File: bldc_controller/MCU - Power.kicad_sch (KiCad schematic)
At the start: 11 parts, among them U1 STM32G474RET3

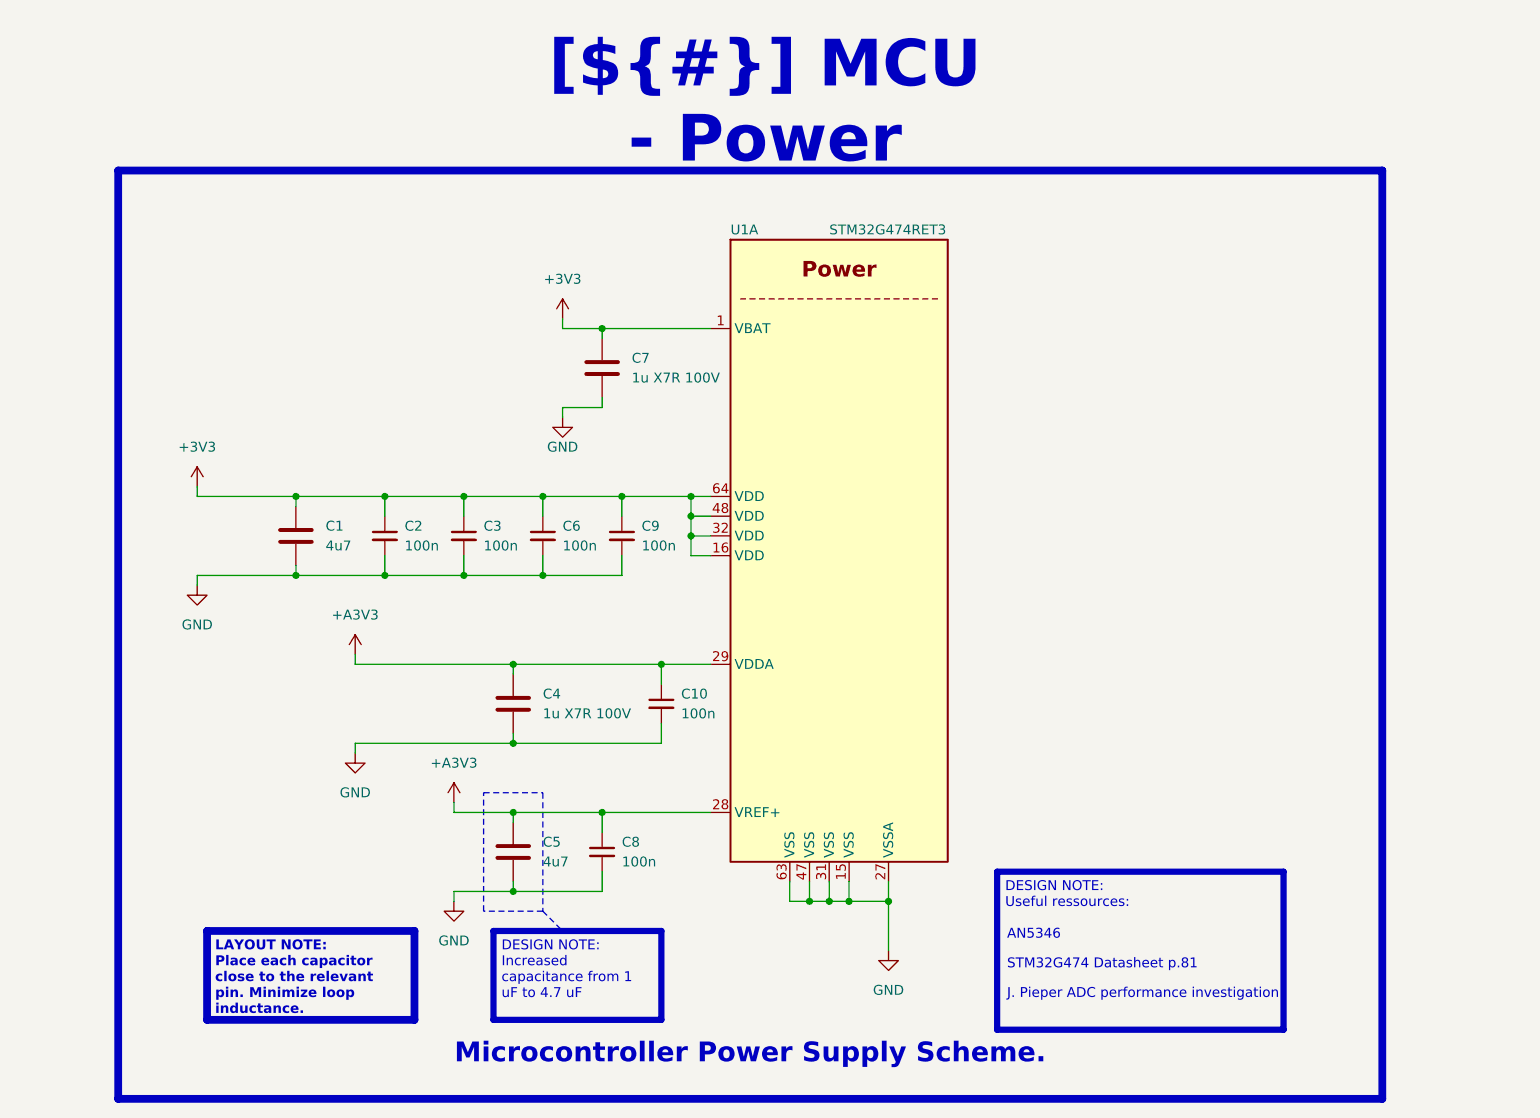
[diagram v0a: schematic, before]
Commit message: schematic is complete. Replaced 5V buck and added pi filters.
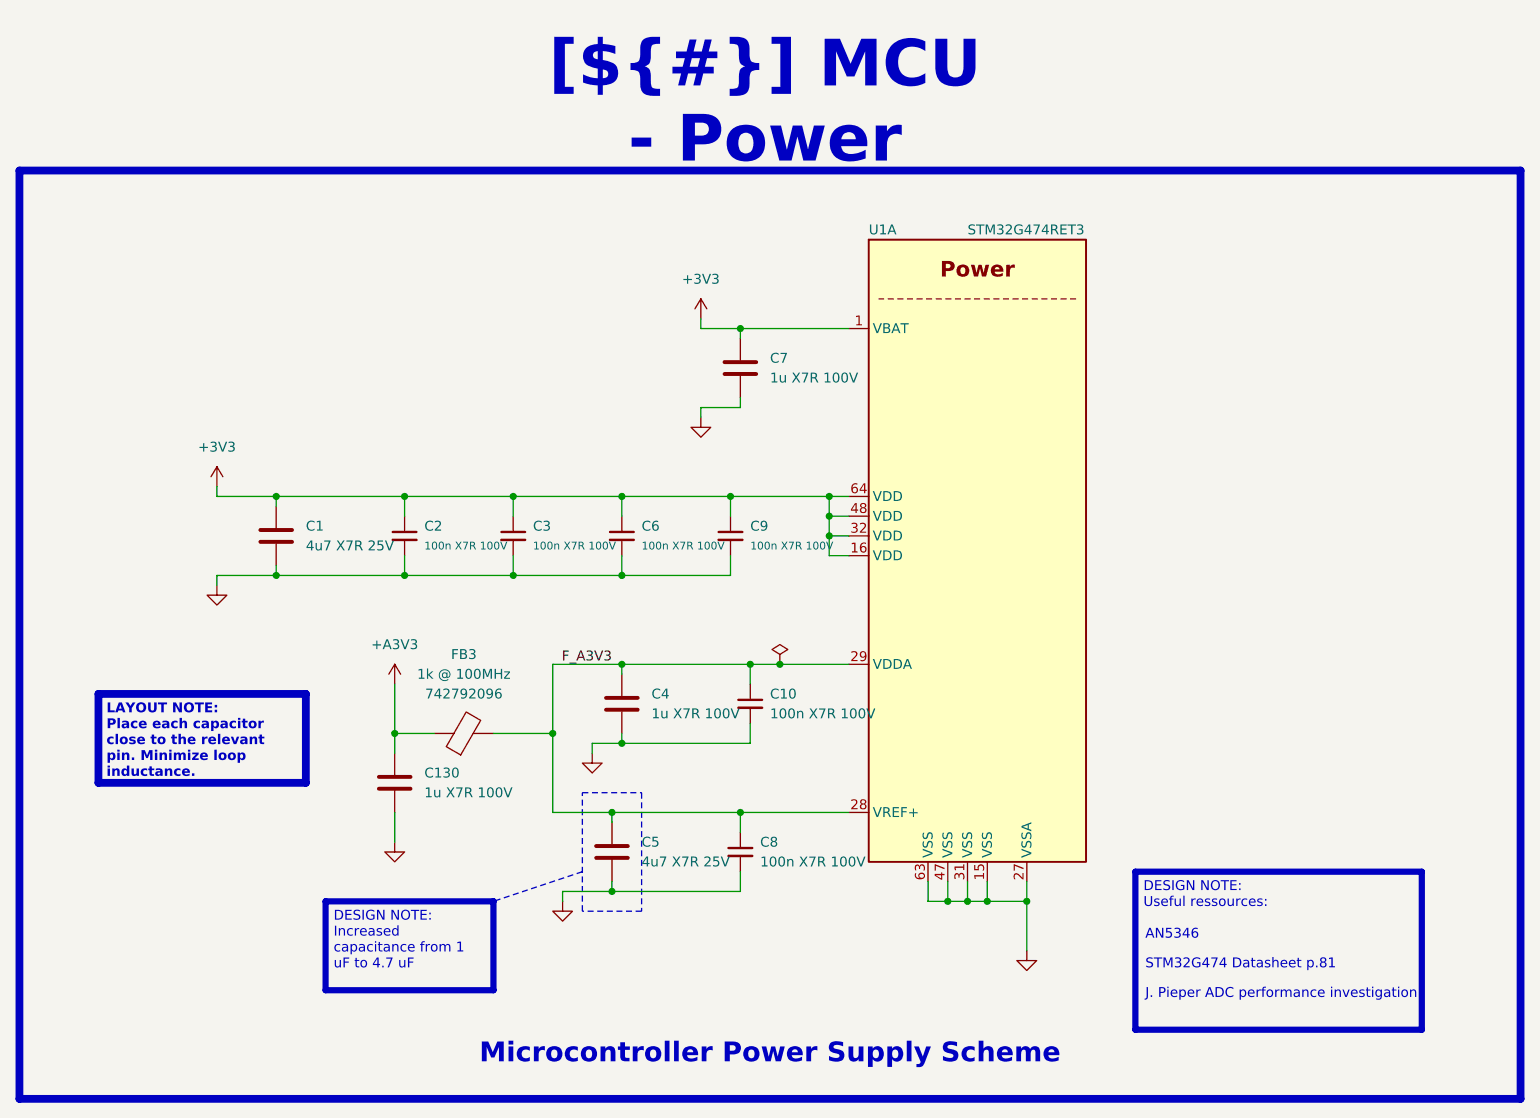
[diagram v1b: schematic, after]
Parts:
- added C130: 1u X7R 100V, 0_capacitor_smd:C_0402_1005_DensityHigh, symbol Device:C
- added FB3: 1k @ 100MHz, 0_resistor_smd:R_0805_2012_DensityHigh, symbol Device:FerriteBead
- C1, C5: value 4u7 -> 4u7 X7R 25V
- C10, C2, C3, C6, C8, C9: value 100n -> 100n X7R 100V
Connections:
- net +A3V3: now also C130.1, FB3.1; no longer C10.1, C4.1, C5.1, C8.1, U1.28 (VREF+), U1.29 (VDDA)
- net GND: now also C130.2
- new net F_A3V3: C10.1, C4.1, C5.1, C8.1, FB3.2, U1.28 (VREF+), U1.29 (VDDA)
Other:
- moved on the sheet: C1, C10, C2, C3, C4, C5, C6, C7, C8, C9, U1A
